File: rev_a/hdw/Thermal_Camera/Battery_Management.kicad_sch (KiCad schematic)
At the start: 38 parts

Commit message: blah blah
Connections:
- net BATT_NTC renamed BATT_NTC1
- net BATT_NTC1: no longer R?.2, U?.10 (BIN)
- new net BATT_NTC2: R?.2, U?.10 (BIN)

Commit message: worked on some battery stuff
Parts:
- removed Q? (x2): BSS214NW, Package_TO_SOT_SMD:SOT-323_SC-70, symbol Transistor_FET:BSS214NW
- added Q? (x2): DMN3042L, Package_TO_SOT_SMD:SOT-23, symbol Transistor_FET:DMN3042L
- added TH? (x2): 10k, symbol Device:Thermistor_NTC
- BT?: Digi-Key PN (none) -> 1568-1488-ND
- L?: value L -> 4.7uH; Ampacity A -> 3.2A; Digi-Key PN (none) -> 541-1222-1-ND; Tolerance Tol -> 20%; display_footprint Foot -> IHLP2020
- R?: value R -> 5.9k
- R?: value R -> 1.2k
- U?: value MAX8903 -> MAX8903G
- U?: value BQ297xy -> BQ29700
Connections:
- net GND: now also Q?.2 (S), TH?.2, TH?.2
- net at C?.1, J?.2 (-), U?.4 (VSS): now also Q?.2 (S)
- net at U?.2 (Cout): now also Q?.1 (G)
- net at U?.3 (Dout): now also Q?.1 (G)
- net BATT_NTC1: no longer names the net of R?.2, U?.16 (THM)
- net BATT_NTC1: now also TH?.1
- net BATT_NTC2: no longer names the net of R?.2, U?.10 (BIN)
- net BATT_NTC2: now also TH?.1
- new net: Q?.3 (D), Q?.3 (D)
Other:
- note added: "4.2V"
- note added: "4.325V"
- note removed: "Determine specific version of each chip to use"
- note removed: "This fuel gauge is sketchy Want to find battery with NTC"

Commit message: some stuff
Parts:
- removed C?: C, Capacitors_SMD:C_0603, symbol Custom_Library:C_Custom
- added C?: 0.1uF, Capacitors_SMD:C_0603, symbol Custom_Library:C_Custom
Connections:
- net GND: now also C?.2
- net at U?.10 (CT): now also C?.1
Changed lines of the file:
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@@
 	(symbol
 		(lib_id "Custom_Library:C_Custom")
+		(at 63.5 137.16 0)
+		(mirror y)
+		(unit 1)
+		(exclude_from_sim no)
+		(in_bom yes)
+		(on_board yes)
+		(dnp no)
+		(property "Reference" "C?"
+			(at 62.865 134.62 0)
+			(effects
+				(font
+					(size 1.27 1.27)
+				)
+				(justify left)
+			)
+		)
+		(property "Value" "0.1uF"
+			(at 62.865 139.7 0)
+			(effects
+				(font
+					(size 1.27 1.27)
+				)
+				(justify left)
+			)
+		)
+		(property "Footprint" "Capacitors_SMD:C_0603"
+			(at 62.5348 140.97 0)
+			(effects
+				(font
+					(size 1.27 1.27)
+				)
+				(hide yes)
+			)
+		)
+		(property "Datasheet" ""
+			(at 62.865 134.62 0)
+			(effects
+				(font
+					(size 1.27 1.27)
+				)
+				(hide yes)
+			)
+		)
+		(property "Description" ""
+			(at 63.5 137.16 0)
+			(effects
+				(font
+					(size 1.27 1.27)
+				)
+				(hide yes)
+			)
+		)
+		(property "Digi-Key PN" "1276-1935-1-ND"
+			(at 52.705 124.46 0)
+			(effects
+				(font
+					(size 1.524 1.524)
+				)
+				(hide yes)
+			)
+		)
+		(property "display_footprint" "0603"
+			(at 67.31 134.62 0)
+			(effects
+				(font
+					(size 1.27 1.27)
+				)
+				(justify right)
+			)
+		)
+		(property "Voltage" "50V"
+			(at 67.31 137.16 0)
+			(effects
+				(font
+					(size 1.27 1.27)
+				)
+				(justify right)
+			)
+		)
+		(property "Dielectric" "X7R"
+			(at 67.31 139.7 0)
+			(effects
+				(font
+					(size 1.27 1.27)
+				)
+				(justify right)
+			)
+		)
+		(pin "1"
+		)
+		(pin "2"
+		)
+		(instances
+			(project "Thermal_Camera"
+				(path "/4bd21e0b-5408-4b93-866e-c82ac5b31fa9/079d68a7-d67d-4f5f-9c02-dfffe75c3c82"
+					(reference "C?")
+					(unit 1)
+				)
+			)
+		)
+	)
+	(symbol
+		(lib_id "Custom_Library:C_Custom")
 		(at 142.24 60.96 0)
 		(mirror y)
@@
 					(unit 1)
 				)
-			)
-		)
-	)
-	(symbol
-		(lib_id "Custom_Library:C_Custom")
-		(at 63.5 137.16 0)
-		(mirror y)
-		(unit 1)
-		(exclude_from_sim no)
-		(in_bom yes)
-		(on_board yes)
-		(dnp no)
-		(property "Reference" "C?"
-			(at 62.865 134.62 0)
-			(effects
-				(font
-					(size 1.27 1.27)
-				)
-				(justify left)
-			)
-		)
-		(property "Value" "C"
-			(at 62.865 139.7 0)
-			(effects
-				(font
-					(size 1.27 1.27)
-				)
-				(justify left)
-			)
-		)
-		(property "Footprint" "Capacitors_SMD:C_0603"
-			(at 62.5348 140.97 0)
-			(effects
-				(font
-					(size 1.27 1.27)
-				)
-				(hide yes)
-			)
-		)
-		(property "Datasheet" ""
-			(at 62.865 134.62 0)
-			(effects
-				(font
-					(size 1.27 1.27)
-				)
-				(hide yes)
-			)
-		)
-		(property "Description" ""
-			(at 63.5 137.16 0)
-			(effects
-				(font
-					(size 1.27 1.27)
-				)
-				(hide yes)
-			)
-		)
-		(property "Digi-Key PN" ""
-			(at 52.705 124.46 0)
-			(effects
-				(font
-					(size 1.524 1.524)
-				)
-				(hide yes)
-			)
-		)
-		(property "display_footprint" "0603"
-			(at 67.31 134.62 0)
-			(effects
-				(font
-					(size 1.27 1.27)
-				)
-				(justify right)
-			)
-		)
-		(property "Voltage" "50V"
-			(at 67.31 137.16 0)
-			(effects
-				(font
-					(size 1.27 1.27)
-				)
-				(justify right)
-			)
-		)
-		(property "Dielectric" "X7R"
-			(at 67.31 139.7 0)
-			(effects
-				(font
-					(size 1.27 1.27)
-				)
-				(justify right)
-			)
-		)
-		(pin "1"
-		)
-		(pin "2"
-		)
-		(instances
-			(project "Thermal_Camera"
-				(path "/4bd21e0b-5408-4b93-866e-c82ac5b31fa9/079d68a7-d67d-4f5f-9c02-dfffe75c3c82"
-					(reference "C?")
-					(unit 1)
-				)
-			)
-			(project "LED_Panel_Controller"
-				(path "/9a153a92-537f-48f9-b716-589877e287a5/00000000-0000-0000-0000-00005baae1cb"
-					(reference "C?")
-					(unit 1)
-				)
-				(path "/9a153a92-537f-48f9-b716-589877e287a5/00000000-0000-0000-0000-00005cad2d97"
-					(reference "C?")
-					(unit 1)
-				)
-				(path "/9a153a92-537f-48f9-b716-589877e287a5/00000000-0000-0000-0000-00005e6af016"
-					(reference "C?")
-					(unit 1)
-				)
-				(path "/9a153a92-537f-48f9-b716-589877e287a5/00000000-0000-0000-0000-00005f582e50"
-					(reference "C?")
-					(unit 1)
-				)
-				(path "/9a153a92-537f-48f9-b716-589877e287a5/00000000-0000-0000-0000-00005baae1f3"
-					(reference "C?")
-					(unit 1)
-				)
-				(path "/9a153a92-537f-48f9-b716-589877e287a5/00000000-0000-0000-0000-00005cb7a8bc"
-					(reference "C?")
-					(unit 1)
-				)
-				(path "/9a153a92-537f-48f9-b716-589877e287a5/00000000-0000-0000-0000-00005f5829c2"
-					(reference "C?")
-					(unit 1)
-				)
-				(path "/9a153a92-537f-48f9-b716-589877e287a5/00000000-0000-0000-0000-00005eae4ae4"
-					(reference "C?")
-					(unit 1)
-				)
-				(path "/9a153a92-537f-48f9-b716-589877e287a5/00000000-0000-0000-0000-00005be48f98"
-					(reference "C?")
-					(unit 1)
-				)
-			)
-			(project "USB_Hub"
-				(path "/e85aac8c-404c-45dd-bda3-1057cae83baf/00000000-0000-0000-0000-00005f41a859"
-					(reference "C?")
-					(unit 1)
-				)
-				(path "/e85aac8c-404c-45dd-bda3-1057cae83baf/00000000-0000-0000-0000-00005f41a7ad"
-					(reference "C202")
-					(unit 1)
-				)

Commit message: lots of schematic progress
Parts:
- C1401, C1408, C1411: renamed from C?; footprint Capacitors_SMD:C_0603 -> (none); display_footprint 0603 -> (none)
- C1403, C1406: renamed from C?; footprint Capacitors_SMD:C_0603 -> (none); Digi-Key PN 399-8153-1-ND -> (none); display_footprint 0603 -> (none)
- C1405, C1407, C1414: renamed from C?; footprint Capacitors_SMD:C_0603 -> (none); Digi-Key PN 1276-1935-1-ND -> (none); display_footprint 0603 -> (none)
- R1401, R1402, R1403, R1406, R1411, R1414, R1415: renamed from R?; footprint Resistors_SMD:R_0603 -> (none); Wattage 1/10W -> (none); display_footprint 0603 -> (none)
- R1407, R1410: renamed from R?; footprint Resistors_SMD:R_0603 -> (none); Digi-Key PN 541-10.0KHCT-ND -> (none); Wattage 1/10W -> (none); display_footprint 0603 -> (none)
- R? (x4): footprint Resistors_SMD:R_0603 -> (none); Digi-Key PN 541-100KHCT-ND -> (none); Wattage 1/10W -> (none); display_footprint 0603 -> (none)
- gave numbers to parts that had none: 17

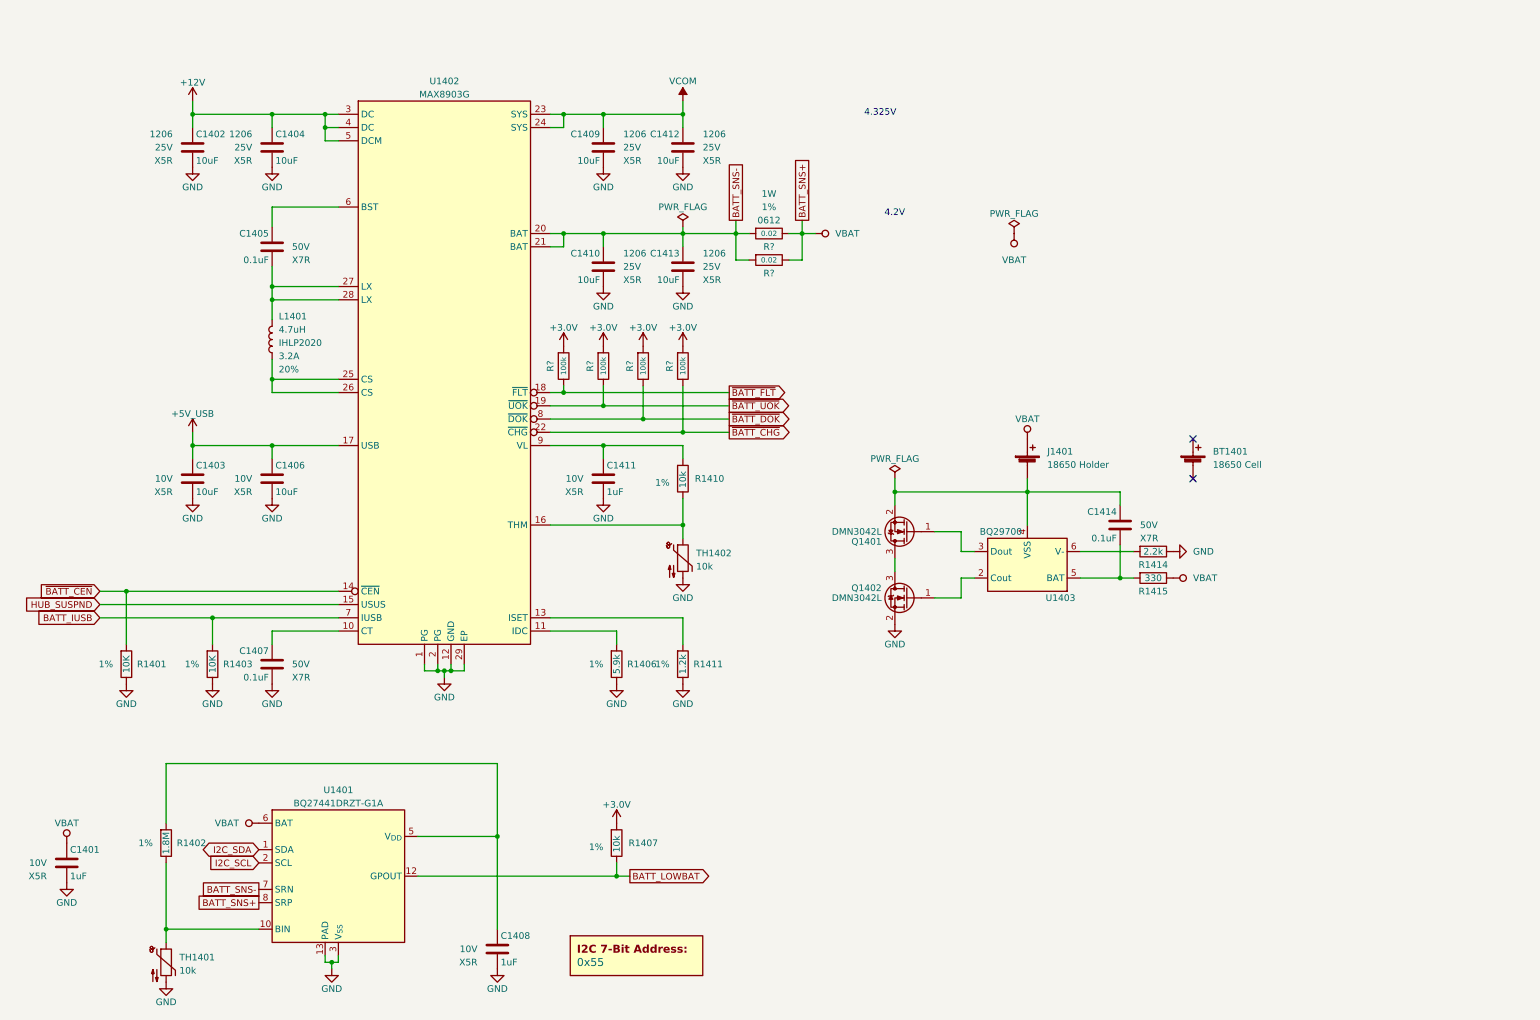
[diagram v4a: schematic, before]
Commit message: assigned a ton of footprints
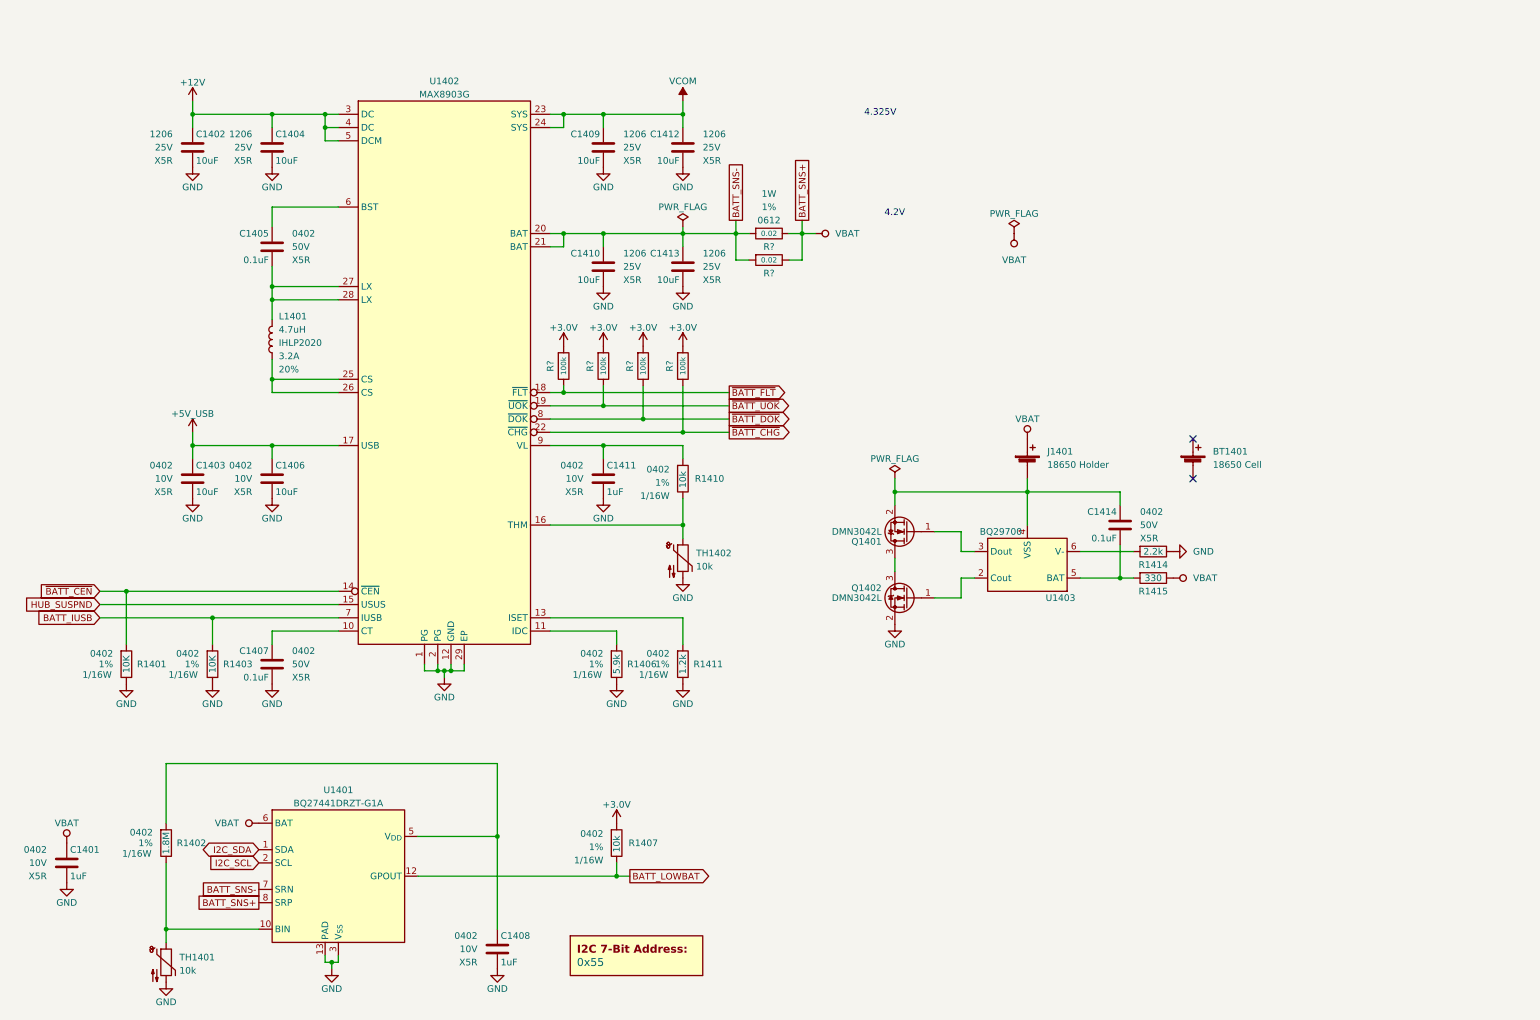
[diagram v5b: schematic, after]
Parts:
- C1401, C1403, C1406, C1408, C1411: footprint (none) -> Capacitors_SMD:C_0402; display_footprint (none) -> 0402
- C1405, C1407, C1414: footprint (none) -> Capacitors_SMD:C_0402; Dielectric X7R -> X5R; display_footprint (none) -> 0402
- J1401: footprint (none) -> Battery:BatteryHolder_MPD_BH-18650-PC2
- R1401, R1402, R1403, R1406, R1407, R1410, R1411, R1414, R1415, R? (x4): footprint (none) -> Resistors_SMD:R_0402; Wattage (none) -> 1/16W; display_footprint (none) -> 0402
- TH1401, TH1402: footprint (none) -> Resistors_SMD:R_0402; display_footprint (none) -> 0402
- U1401: Digi-Key PN (none) -> 296-37271-1-ND
- U1402: Digi-Key PN (none) -> MAX8903GETI+-ND
- U1403: Digi-Key PN (none) -> 296-43985-1-ND

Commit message: assigned some part numbers
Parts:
- C1401, C1408, C1411: Digi-Key PN (none) -> 311-1439-1-ND
- C1403, C1406: Digi-Key PN (none) -> 490-GRM155R61A106ME11DCT-ND
- C1405, C1407, C1414: Digi-Key PN (none) -> 490-10697-1-ND
- J1401: Digi-Key PN (none) -> BK-18650-PC2-ND
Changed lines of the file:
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@@
 			)
 		)
-		(property "Digi-Key PN" ""
+		(property "Digi-Key PN" "490-10697-1-ND"
 			(at 215.265 97.79 0)
 			(effects
@@
 			)
 		)
-		(property "Digi-Key PN" ""
+		(property "Digi-Key PN" "490-GRM155R61A106ME11DCT-ND"
 			(at 48.26 101.6 0)
 			(effects
@@
 			)
 		)
+		(property "Digi-Key PN" "BK-18650-PC2-ND"
+			(at 208.28 99.06 0)
+			(effects
+				(font
+					(size 1.27 1.27)
+				)
+				(hide yes)
+			)
+		)
 		(pin "1"
 		)
@@
 			)
 		)
-		(property "Digi-Key PN" ""
+		(property "Digi-Key PN" "490-10697-1-ND"
 			(at 52.705 124.46 0)
 			(effects
@@
 			)
 		)
-		(property "Digi-Key PN" ""
+		(property "Digi-Key PN" "311-1439-1-ND"
 			(at 127 101.6 0)
 			(effects
@@
 			)
 		)
-		(property "Digi-Key PN" ""
+		(property "Digi-Key PN" "490-GRM155R61A106ME11DCT-ND"
 			(at 63.5 101.6 0)
 			(effects
@@
 			)
 		)
-		(property "Digi-Key PN" ""
+		(property "Digi-Key PN" "490-10697-1-ND"
 			(at 52.705 44.45 0)
 			(effects
@@
 			)
 		)
-		(property "Digi-Key PN" ""
+		(property "Digi-Key PN" "311-1439-1-ND"
 			(at 24.13 175.26 0)
 			(effects
@@
 			)
 		)
-		(property "Digi-Key PN" ""
+		(property "Digi-Key PN" "311-1439-1-ND"
 			(at 106.68 191.77 0)
 			(effects

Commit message: assigned resistor part numbers
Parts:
- Q1401, Q1402: Digi-Key PN (none) -> DMN3042L-7DICT-ND
- R1401, R1403, R1407, R1410: Digi-Key PN (none) -> RMCF0402FT10K0CT-ND
- R1402: Digi-Key PN (none) -> RMCF0402FT1M80CT-ND
- R1406: Digi-Key PN (none) -> RMCF0402FT5K90CT-ND
- R1411: Digi-Key PN (none) -> RMCF0402FT1K20CT-ND
- R1414: Digi-Key PN (none) -> RMCF0402FT2K20CT-ND
- R1415: Digi-Key PN (none) -> RMCF0402FT330RCT-ND
- R? (x4): Digi-Key PN (none) -> RMCF0402FT100KCT-ND
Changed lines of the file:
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@@
 			)
 		)
-		(property "Digi-Key PN" ""
+		(property "Digi-Key PN" "RMCF0402FT5K90CT-ND"
 			(at 121.92 127 0)
 			(effects
@@
 			)
 		)
-		(property "Digi-Key PN" ""
+		(property "Digi-Key PN" "RMCF0402FT2K20CT-ND"
 			(at 222.25 107.95 0)
 			(effects
@@
 			)
 		)
+		(property "Digi-Key PN" "DMN3042L-7DICT-ND"
+			(at 185.42 111.76 0)
+			(effects
+				(font
+					(size 1.27 1.27)
+				)
+				(hide yes)
+			)
+		)
 		(pin "2"
 		)
@@
 			)
 		)
+		(property "Digi-Key PN" "DMN3042L-7DICT-ND"
+			(at 185.42 124.46 0)
+			(effects
+				(font
+					(size 1.27 1.27)
+				)
+				(hide yes)
+			)
+		)
 		(pin "2"
 		)
@@
 			)
 		)
-		(property "Digi-Key PN" ""
+		(property "Digi-Key PN" "RMCF0402FT100KCT-ND"
 			(at 119.38 80.01 0)
 			(effects
@@
 			)
 		)
-		(property "Digi-Key PN" ""
+		(property "Digi-Key PN" "RMCF0402FT1M80CT-ND"
 			(at 35.56 161.29 0)
 			(effects
@@
 			)
 		)
-		(property "Digi-Key PN" ""
+		(property "Digi-Key PN" "RMCF0402FT10K0CT-ND"
 			(at 134.62 91.44 0)
 			(effects
@@
 			)
 		)
-		(property "Digi-Key PN" ""
+		(property "Digi-Key PN" "RMCF0402FT100KCT-ND"
 			(at 127 80.01 0)
 			(effects
@@
 			)
 		)
-		(property "Digi-Key PN" ""
+		(property "Digi-Key PN" "RMCF0402FT330RCT-ND"
 			(at 222.25 113.03 0)
 			(effects
@@
 			)
 		)
-		(property "Digi-Key PN" ""
+		(property "Digi-Key PN" "RMCF0402FT10K0CT-ND"
 			(at 44.45 127 0)
 			(effects
@@
 			)
 		)
-		(property "Digi-Key PN" ""
+		(property "Digi-Key PN" "RMCF0402FT1K20CT-ND"
 			(at 134.62 127 0)
 			(effects
@@
 			)
 		)
-		(property "Digi-Key PN" ""
+		(property "Digi-Key PN" "RMCF0402FT10K0CT-ND"
 			(at 27.94 127 0)
 			(effects
@@
 			)
 		)
-		(property "Digi-Key PN" ""
+		(property "Digi-Key PN" "RMCF0402FT100KCT-ND"
 			(at 142.24 80.01 0)
 			(effects
@@
 			)
 		)
-		(property "Digi-Key PN" ""
+		(property "Digi-Key PN" "RMCF0402FT10K0CT-ND"
 			(at 121.92 161.29 0)
 			(effects
@@
 			)
 		)
-		(property "Digi-Key PN" ""
+		(property "Digi-Key PN" "RMCF0402FT100KCT-ND"
 			(at 134.62 80.01 0)
 			(effects

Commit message: lots of PCB placement progress
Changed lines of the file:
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@@
 	(wire
 		(pts
-			(xy 165.1 52.07) (xy 165.1 54.61)
-		)
-		(stroke
-			(width 0)
-			(type default)
-		)
-	)
-	(wire
-		(pts
 			(xy 96.52 138.43) (xy 95.25 138.43)
 		)
@@
 		)
 	)
-	(global_label "BATT_SNS+"
-		(shape passive)
-		(at 165.1 52.07 90)
-		(fields_autoplaced yes)
-		(effects
-			(font
-				(size 1.27 1.27)
-			)
-			(justify left)
-		)
-		(property "Intersheetrefs" "${INTERSHEET_REFS}"
-			(at 165.1 39.6922 90)
-			(effects
-				(font
-					(size 1.27 1.27)
-				)
-				(justify left)
-				(hide yes)
-			)
-		)
-	)
 	(global_label "BATT_SNS-"
 		(shape passive)
@@
 		)
 	)
-	(global_label "BATT_SNS+"
-		(shape passive)
-		(at 60.96 182.88 180)
-		(fields_autoplaced yes)
-		(effects
-			(font
-				(size 1.27 1.27)
-			)
-			(justify right)
-		)
-		(property "Intersheetrefs" "${INTERSHEET_REFS}"
-			(at 48.5822 182.88 0)
-			(effects
-				(font
-					(size 1.27 1.27)
-				)
-				(justify right)
-				(hide yes)
-			)
-		)
-	)
 	(global_label "~{BATT_CHG}"
 		(shape output)
@@
 					(unit 1)
 				)
+			)
+		)
+	)
+	(symbol
+		(lib_id "Custom Library:VBAT")
+		(at 60.96 182.88 90)
+		(unit 1)
+		(exclude_from_sim no)
+		(in_bom yes)
+		(on_board yes)
+		(dnp no)
+		(fields_autoplaced yes)
+		(property "Reference" "#PWR01437"
+			(at 64.77 182.88 0)
+			(effects
+				(font
+					(size 1.27 1.27)
+				)
+				(hide yes)
+			)
+		)
+		(property "Value" "VBAT"
+			(at 57.15 182.8799 90)
+			(effects
+				(font
+					(size 1.27 1.27)
+				)
+				(justify left)
+			)
+		)
+		(property "Footprint" ""
+			(at 60.96 182.88 0)
+			(effects
+				(font
+					(size 1.27 1.27)
+				)
+				(hide yes)
+			)
+		)
+		(property "Datasheet" ""
+			(at 60.96 182.88 0)
+			(effects
+				(font
+					(size 1.27 1.27)
+				)
+				(hide yes)
+			)
+		)
+		(property "Description" ""
+			(at 60.96 182.88 0)
+			(effects
+				(font
+					(size 1.27 1.27)
+				)
+				(hide yes)
+			)
+		)
+		(pin "1"
+		)
+		(instances
+			(project "Thermal_Camera"
+				(path "/4bd21e0b-5408-4b93-866e-c82ac5b31fa9/079d68a7-d67d-4f5f-9c02-dfffe75c3c82"
+					(reference "#PWR01437")
+					(unit 1)
+				)
